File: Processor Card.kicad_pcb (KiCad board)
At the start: 2 copper layers, 100 x 100 mm, 33 parts, among them J1 Serial Port, J2 Conn_02x20_Odd_Even, U1 74LS32, U2 74LS04, U3 28C256 / 62256, U4 74LS73, U5 28C256 / 62256, U6 CDP1802/1806, U7 74LS373, U8 74LS138

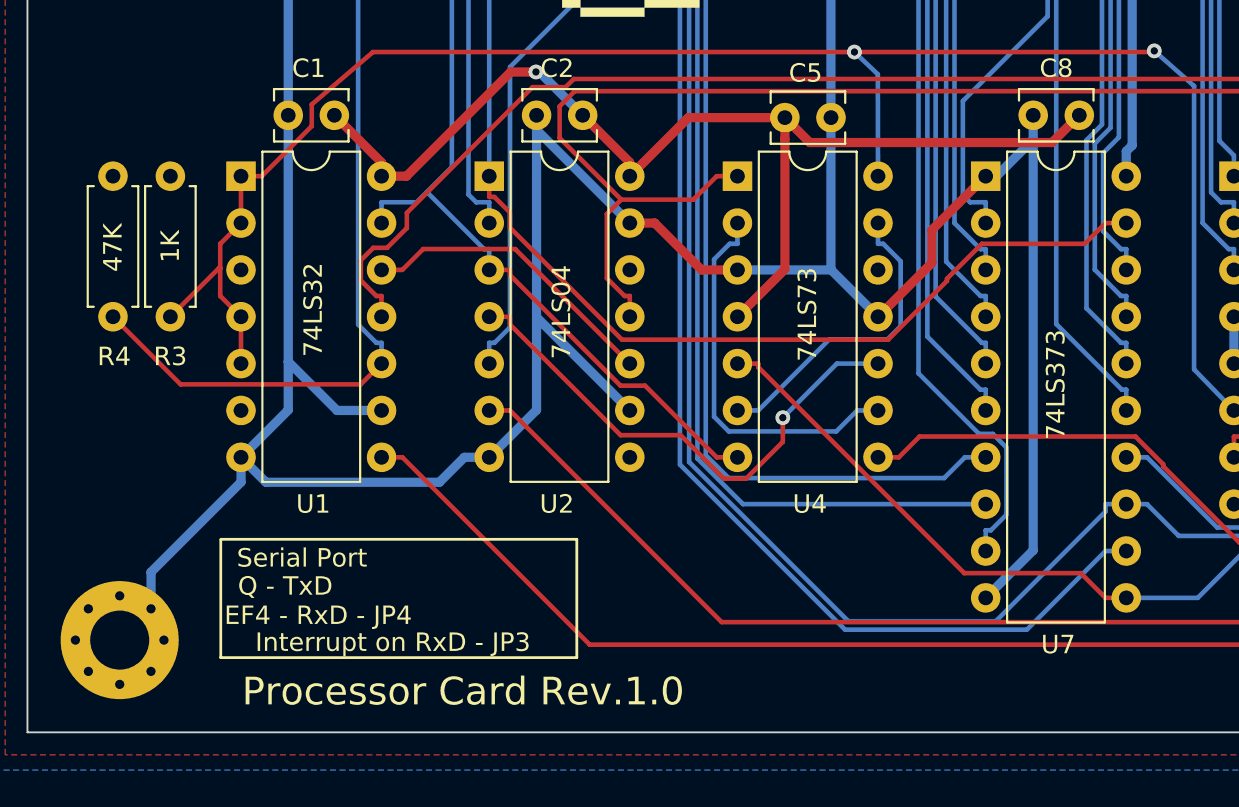
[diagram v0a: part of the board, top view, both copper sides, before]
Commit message: Added Gate Delay to IO Decode
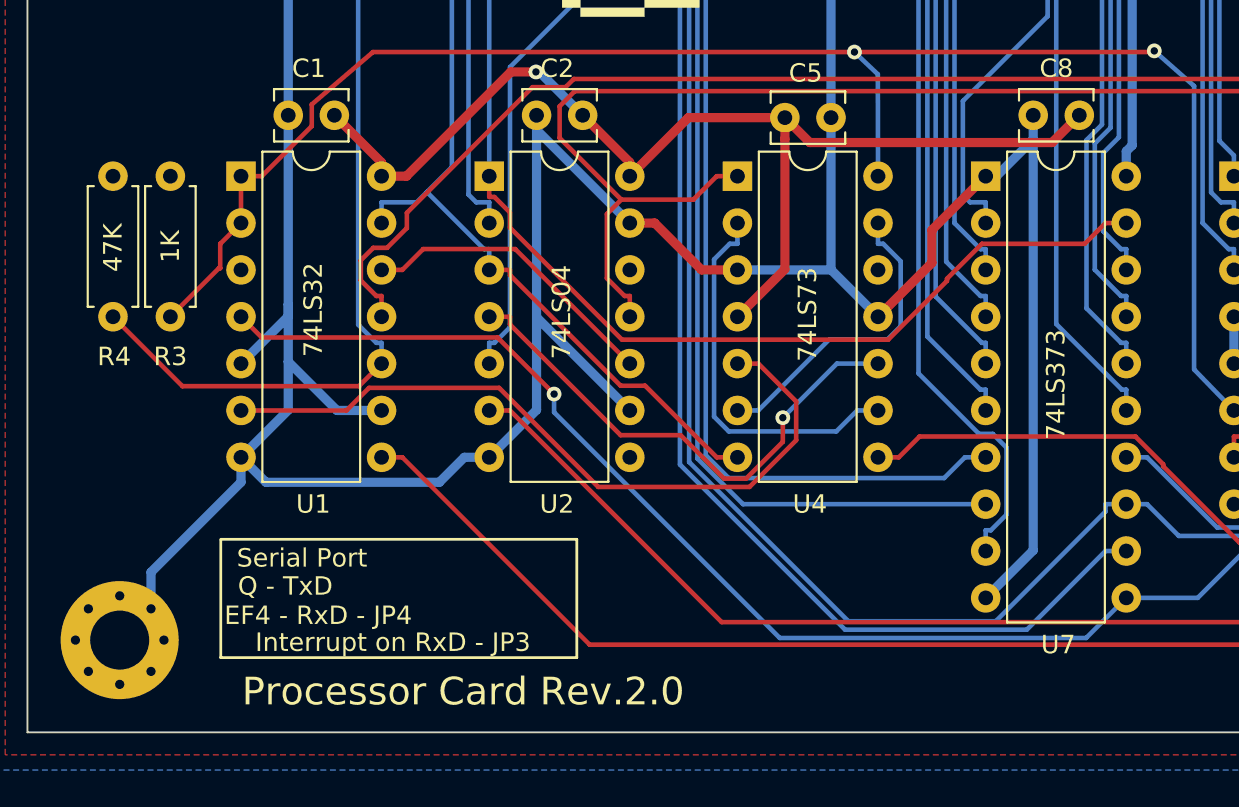
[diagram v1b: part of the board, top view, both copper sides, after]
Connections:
- U1 pad 4: HI -> TPA
- U1 pad 5: HI -> GND
- U4 pad 5: TPA -> Net-(U1-Pad6)
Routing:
- net Net-(U1-Pad6): track 0.00 -> 40.0 mm
- net TPA: track 121.1 -> 151.4 mm, vias 0 -> 1
- net HI: track 96.4 -> 90.8 mm
- net GND: track 508.8 -> 513.0 mm
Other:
- board text added: "Processor Card Rev.2.0"
- board text removed: "Processor Card Rev.1.0"
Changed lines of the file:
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@@
     (thickness 1.6)
     (drawings 23)
-    (tracks 1131)
+    (tracks 1142)
     (zones 0)
     (modules 33)
@@
       (net 67 "Net-(U4-Pad12)"))
     (pad 5 thru_hole oval (at 0 10.16) (size 1.6 1.6) (drill 0.8) (layers *.Cu *.Mask)
-      (net 20 TPA))
+      (net 72 "Net-(U1-Pad6)"))
     (pad 11 thru_hole oval (at 7.62 7.62) (size 1.6 1.6) (drill 0.8) (layers *.Cu *.Mask)
       (net 2 GND))
@@
       (net 69 "Net-(U1-Pad12)"))
     (pad 5 thru_hole oval (at 0 10.16) (size 1.6 1.6) (drill 0.8) (layers *.Cu *.Mask)
-      (net 78 HI))
+      (net 2 GND))
     (pad 11 thru_hole oval (at 7.62 7.62) (size 1.6 1.6) (drill 0.8) (layers *.Cu *.Mask)
       (net 10 ~IOW))
     (pad 4 thru_hole oval (at 0 7.62) (size 1.6 1.6) (drill 0.8) (layers *.Cu *.Mask)
-      (net 78 HI))
+      (net 20 TPA))
     (pad 10 thru_hole oval (at 7.62 10.16) (size 1.6 1.6) (drill 0.8) (layers *.Cu *.Mask)
       (net 75 /RX))
@@
     (effects (font (size 1 1) (thickness 0.15)))
   )
-  (gr_text "Processor Card Rev.1.0" (at 123.622 147.79) (layer F.SilkS)
+  (gr_text "Processor Card Rev.2.0" (at 123.622 147.79) (layer F.SilkS)
     (effects (font (size 1.5 1.5) (thickness 0.3)))
   )
@@
   (segment (start 119.196 132.55) (end 116.7805 132.55) (width 0.5) (layer B.Cu) (net 2) (status 10))
   (segment (start 114.137 129.9065) (end 114.137 132.529) (width 0.5) (layer B.Cu) (net 2))
-  (segment (start 114.137 116.548) (end 114.137 129.9065) (width 0.5) (layer B.Cu) (net 2) (status 10))
   (segment (start 112.9293 136.4433) (end 111.576 135.09) (width 0.5) (layer B.Cu) (net 2) (status 20))
   (segment (start 123.6827 135.09) (end 122.3294 136.4433) (width 0.5) (layer B.Cu) (net 2))
   (segment (start 122.3294 136.4433) (end 112.9293 136.4433) (width 0.5) (layer B.Cu) (net 2))
   (segment (start 125.033 135.09) (end 123.6827 135.09) (width 0.5) (layer B.Cu) (net 2) (status 10))
+  (segment (start 114.137 127.449) (end 114.137 126.795) (width 0.5) (layer B.Cu) (net 2))
+  (segment (start 111.576 130.01) (end 114.137 127.449) (width 0.5) (layer B.Cu) (net 2))
+  (segment (start 114.137 126.795) (end 114.137 129.9065) (width 0.5) (layer B.Cu) (net 2))
+  (segment (start 114.137 116.548) (end 114.137 126.795) (width 0.5) (layer B.Cu) (net 2))
   (segment (start 167.209 58.8256) (end 170.5633 55.4713) (width 0.5) (layer B.Cu) (net 3))
   (segment (start 170.5633 55.4713) (end 173.4163 55.4713) (width 0.5) (layer B.Cu) (net 3))
@@
   (segment (start 181.095 75.432) (end 181.095 76.5573) (width 0.25) (layer B.Cu) (net 20) (status 10))
   (segment (start 195.94 90.037) (end 195.3524 90.037) (width 0.25) (layer B.Cu) (net 20) (status 30))
-  (segment (start 138.49 130.01) (end 139.6153 130.01) (width 0.25) (layer F.Cu) (net 20) (status 10))
-  (segment (start 159.568 142.71) (end 158.4427 142.71) (width 0.25) (layer F.Cu) (net 20) (status 10))
-  (segment (start 158.4427 142.71) (end 157.102 141.3693) (width 0.25) (layer F.Cu) (net 20))
-  (segment (start 157.102 141.3693) (end 150.7856 141.3693) (width 0.25) (layer F.Cu) (net 20))
-  (segment (start 150.7856 141.3693) (end 139.6153 130.199) (width 0.25) (layer F.Cu) (net 20))
-  (segment (start 139.6153 130.199) (end 139.6153 130.01) (width 0.25) (layer F.Cu) (net 20))
+  (via (at 128.549 131.661) (size 0.8) (drill 0.4) (layers F.Cu B.Cu) (net 20))
+  (segment (start 128.549 132.651002) (end 128.549 131.661) (width 0.25) (layer B.Cu) (net 20))
+  (segment (start 140.782508 144.88451) (end 128.549 132.651002) (width 0.25) (layer B.Cu) (net 20))
+  (segment (start 157.39349 144.88451) (end 140.782508 144.88451) (width 0.25) (layer B.Cu) (net 20))
+  (segment (start 159.568 142.71) (end 157.39349 144.88451) (width 0.25) (layer B.Cu) (net 20))
+  (segment (start 112.701001 128.595001) (end 111.576 127.47) (width 0.25) (layer F.Cu) (net 20))
+  (segment (start 125.483001 128.595001) (end 112.701001 128.595001) (width 0.25) (layer F.Cu) (net 20))
+  (segment (start 128.549 131.661) (end 125.483001 128.595001) (width 0.25) (layer F.Cu) (net 20))
   (segment (start 155.3053 75.432) (end 157.8729 77.9996) (width 0.25) (layer F.Cu) (net 21))
   (segment (start 157.8729 77.9996) (end 162.1621 77.9996) (width 0.25) (layer F.Cu) (net 21))
@@
   (segment (start 195.5712 60.1462) (end 196.4877 61.0627) (width 0.25) (layer F.Cu) (net 70))
   (segment (start 196.4877 61.0627) (end 196.4877 61.43) (width 0.25) (layer F.Cu) (net 70))
+  (segment (start 117.29241 132.55) (end 111.576 132.55) (width 0.25) (layer F.Cu) (net 72))
+  (segment (start 125.569709 131.324999) (end 118.517411 131.324999) (width 0.25) (layer F.Cu) (net 72))
+  (segment (start 130.94172 136.69701) (end 125.569709 131.324999) (width 0.25) (layer F.Cu) (net 72))
+  (segment (start 118.517411 131.324999) (end 117.29241 132.55) (width 0.25) (layer F.Cu) (net 72))
+  (segment (start 139.1439 136.69701) (end 130.94172 136.69701) (width 0.25) (layer F.Cu) (net 72))
+  (segment (start 141.673601 134.167309) (end 139.1439 136.69701) (width 0.25) (layer F.Cu) (net 72))
+  (segment (start 141.673601 132.062231) (end 141.673601 134.167309) (width 0.25) (layer F.Cu) (net 72))
+  (segment (start 139.62137 130.01) (end 141.673601 132.062231) (width 0.25) (layer F.Cu) (net 72))
+  (segment (start 138.49 130.01) (end 139.62137 130.01) (width 0.25) (layer F.Cu) (net 72))
   (segment (start 181.4046 126.2929) (end 180.137 125.0253) (width 0.25) (layer B.Cu) (net 74))
   (segment (start 179.776 144.0247) (end 179.0116 143.2603) (width 0.25) (layer B.Cu) (net 74))
@@
   (segment (start 184.4733 54.0549) (end 191.4077 60.9893) (width 0.25) (layer B.Cu) (net 75))
   (segment (start 191.4077 60.9893) (end 191.4077 61.43) (width 0.25) (layer B.Cu) (net 75))
-  (segment (start 118.070999 131.135001) (end 119.196 130.01) (width 0.25) (layer F.Cu) (net 75))
-  (segment (start 108.300501 131.135001) (end 118.070999 131.135001) (width 0.25) (layer F.Cu) (net 75))
-  (segment (start 104.6355 127.47) (end 108.300501 131.135001) (width 0.25) (layer F.Cu) (net 75))
+  (segment (start 117.970999 131.235001) (end 119.196 130.01) (width 0.25) (layer F.Cu) (net 75))
+  (segment (start 108.400501 131.235001) (end 117.970999 131.235001) (width 0.25) (layer F.Cu) (net 75))
+  (segment (start 104.6355 127.47) (end 108.400501 131.235001) (width 0.25) (layer F.Cu) (net 75))
   (segment (start 186.106 137.503) (end 186.106 138.6283) (width 0.25) (layer B.Cu) (net 77) (status 10))
   (segment (start 187.396 145.25) (end 187.396 139.9183) (width 0.25) (layer B.Cu) (net 77) (status 10))
   (segment (start 187.396 139.9183) (end 186.106 138.6283) (width 0.25) (layer B.Cu) (net 77))
   (segment (start 111.576 122.39) (end 111.576 119.85) (width 0.25) (layer F.Cu) (net 78))
-  (segment (start 111.576 130.01) (end 111.576 127.47) (width 0.25) (layer F.Cu) (net 78))
   (segment (start 110.450999 123.515001) (end 111.576 122.39) (width 0.25) (layer F.Cu) (net 78))
-  (segment (start 111.576 127.47) (end 110.450999 126.344999) (width 0.25) (layer F.Cu) (net 78))
   (segment (start 110.377001 124.839999) (end 110.450999 124.839999) (width 0.25) (layer F.Cu) (net 78))
   (segment (start 107.747 127.47) (end 110.377001 124.839999) (width 0.25) (layer F.Cu) (net 78))
   (segment (start 110.450999 124.839999) (end 110.450999 123.515001) (width 0.25) (layer F.Cu) (net 78))
-  (segment (start 110.450999 126.344999) (end 110.450999 124.839999) (width 0.25) (layer F.Cu) (net 78))
   (segment (start 112.698 119.85) (end 111.576 119.85) (width 0.25) (layer F.Cu) (net 78))
   (segment (start 115.411999 117.136001) (end 112.698 119.85) (width 0.25) (layer F.Cu) (net 78))

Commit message: Sync
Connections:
- U1 pad 1: HI -> Net-(U1-Pad1)
- U1 pad 2: HI -> Net-(U1-Pad1)
- U1 pad 6: Net-(U1-Pad6) -> Net-(U1-Pad1)
- U4 pad 5: Net-(U1-Pad6) -> Net-(U1-Pad3)
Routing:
- net Net-(U1-Pad3): track 0.00 -> 51.6 mm, vias 0 -> 2
- net Net-(U1-Pad6): track 40.0 -> 0.00 mm
- net Net-(U1-Pad1): track 0.00 -> 13.7 mm
- net HI: track 90.8 -> 91.6 mm
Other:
- board text added: "Processor Card Rev.2.1"
- board text removed: "Processor Card Rev.2.0"

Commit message: Revision 2
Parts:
- removed D2: RED, LED_THT:LED_D3.0mm_Horizontal_O1.27mm_Z2.0mm
- removed the J1 at (185.0, 61.4)
- removed JP1, JP2: RAM ROM, Connector_PinHeader_2.54mm:PinHeader_1x03_P2.54mm_Vertical
- removed JP3: ~INT, Connector_PinHeader_2.54mm:PinHeader_1x02_P2.54mm_Vertical
- removed JP4: ~EF4, Connector_PinHeader_2.54mm:PinHeader_1x02_P2.54mm_Vertical
- removed R3: 1K, Resistor_THT:R_Axial_DIN0207_L6.3mm_D2.5mm_P7.62mm_Horizontal
- removed R4: 47K, Resistor_THT:R_Axial_DIN0207_L6.3mm_D2.5mm_P7.62mm_Horizontal
- removed the U8 at (165.4, 119.8)
- added C10: 100nF, Capacitor_THT:C_Disc_D3.8mm_W2.6mm_P2.50mm, F.Cu at (133.4, 121.8)
- added C11: 100nF, Capacitor_THT:C_Disc_D3.8mm_W2.6mm_P2.50mm, F.Cu at (149.6, 121.8)
- added C9: 100nF, Capacitor_THT:C_Disc_D3.8mm_W2.6mm_P2.50mm, F.Cu at (117.1, 121.8)
- added U10: 74LS573, Package_DIP:DIP-20_W7.62mm, F.Cu at (160.8, 101.4)
- added U11: 74LS138, Package_DIP:DIP-16_W7.62mm, F.Cu at (144.6, 125.6)
- added U3: 62256, Package_DIP:DIP-28_W15.24mm_Socket, F.Cu at (132.4, 59.5)
- added U5: 74LS32, Package_DIP:DIP-14_W7.62mm, F.Cu at (144.6, 101.4)
- D1: value GREEN -> LED
- R1: value 470R -> 1K
- U1: value 74LS32 -> CDP1802/1806; footprint Package_DIP:DIP-14_W7.62mm -> Package_DIP:DIP-40_W15.24mm_Socket
- U2: value 74LS04 -> 28C256; footprint Package_DIP:DIP-14_W7.62mm -> Package_DIP:DIP-28_W15.24mm_Socket
- U4: value 74LS73 -> 62256; footprint Package_DIP:DIP-14_W7.62mm -> Package_DIP:DIP-28_W15.24mm_Socket
- U6: renamed from U3; value 28C256 / 62256 -> 74LS20; footprint Package_DIP:DIP-28_W15.24mm_Socket -> Package_DIP:DIP-14_W7.62mm
- U7: value 74LS373 -> 74LS74; footprint Package_DIP:DIP-20_W7.62mm -> Package_DIP:DIP-14_W7.62mm
- U8: renamed from U5; value 28C256 / 62256 -> 74LS04; footprint Package_DIP:DIP-28_W15.24mm_Socket -> Package_DIP:DIP-14_W7.62mm
- U9: renamed from U6; value CDP1802/1806 -> 74LS74; footprint Package_DIP:DIP-40_W15.24mm_Socket -> Package_DIP:DIP-14_W7.62mm
- moved U1 86.1 mm to (173.0, 59.5)
- moved U6 70.7 mm to (112.1, 125.6)
- moved U4 62.0 mm to (152.7, 59.5)
- moved C4 61.9 mm to (181.9, 55.7)
- moved C2 61.8 mm to (141.3, 55.7)
- moved U2 61.7 mm to (112.1, 59.5)
- moved C1 61.0 mm to (120.9, 55.7)
- moved U9 55.8 mm to (128.3, 101.4)
- moved G*** 50.2 mm to (176.2, 135.1)
- moved C7 47.9 mm to (149.6, 97.6)
- moved C6 42.7 mm to (133.4, 97.6)
- moved U8 41.2 mm to (112.1, 101.4)
- moved C5 30.6 mm to (117.1, 97.6), turned to 180 degrees
- moved U7 24.3 mm to (128.3, 125.6)
- moved C8 20.9 mm to (165.9, 97.6)
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- renumbered C9 to C12, J2 to J1
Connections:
- J1 pad 10: ~INTERRUPT -> ~{INTERRUPT}
- J1 pad 12: ~MWR -> ~{MWR}
- J1 pad 13: ~MRD -> ~{MRD}
- J1 pad 15: Net-(J2-Pad15) -> unconnected-(J1-Pad15)
- J1 pad 25: ~IOW -> ~{IOW}
- J1 pad 26: ~IOR -> ~{IOR}
- J1 pad 27: ~N7 -> ~{N7}
- J1 pad 28: ~N6 -> ~{N6}
- J1 pad 29: ~N5 -> ~{N5}
- J1 pad 3: ~WAIT -> ~{WAIT}
- J1 pad 30: ~N4 -> ~{N4}
- J1 pad 31: ~N3 -> ~{N3}
- J1 pad 32: ~N2 -> ~{N2}
- J1 pad 33: ~N1 -> ~{N1}
- J1 pad 34: Net-(J2-Pad34) -> unconnected-(J1-Pad34)
- J1 pad 35: ~EF1 -> ~{EF1}
- J1 pad 36: ~EF2 -> ~{EF2}
- J1 pad 37: ~EF3 -> ~{EF3}
- J1 pad 38: ~EF4 -> ~{EF4}
- J1 pad 5: ~CLEAR -> ~{CLEAR}
- J1 pad 6: ~DMA_IN -> ~{DMA_IN}
- J1 pad 8: ~DMA_OUT -> ~{DMA_OUT}
- R1 pad 2: Net-(D1-Pad2) -> HI
- R2 pad 2: Net-(D2-Pad2) -> Net-(D1-Pad2)
- U1 pad 1: Net-(U1-Pad1) -> CLOCK
- U1 pad 10: /RX -> D5
- U1 pad 11: ~IOW -> D4
- U1 pad 12: Net-(U1-Pad12) -> D3
- U1 pad 13: ~MRD -> D2
- U1 pad 14: VCC -> D1
- U1 pad 2: Net-(U1-Pad1) -> ~{WAIT}
- U1 pad 3: Net-(U1-Pad3) -> ~{CLEAR}
- U1 pad 4: TPA -> Q
- U1 pad 5: GND -> SC1
- U1 pad 6: Net-(U1-Pad1) -> SC0
- U1 pad 7: GND -> ~{MRD}
- U1 pad 8: Net-(D1-Pad1) -> D7
- U1 pad 9: GND -> D6
- U2 pad 1: /A15 -> /A14
- U2 pad 10: Net-(U1-Pad12) -> /A0
- U2 pad 11: TPB -> D0
- U2 pad 12: Net-(U2-Pad12) -> D1
- U2 pad 13: GND -> D2
- U2 pad 14: VCC -> GND
- U2 pad 2: Net-(U2-Pad2) -> /A12
- U2 pad 3: ~MRD -> /A7
- U2 pad 4: Net-(U2-Pad4) -> /A6
- U2 pad 5: Q -> /A5
- U2 pad 6: /TX -> /A4
- U2 pad 7: GND -> /A3
- U2 pad 8: Net-(U2-Pad8) -> /A2
- U2 pad 9: GND -> /A1
- U4 pad 1: TPB -> /A14
- U4 pad 10: Net-(U2-Pad4) -> /A0
- U4 pad 11: GND -> D0
- U4 pad 12: Net-(U4-Pad12) -> D1
- U4 pad 13: Net-(U4-Pad13) -> D2
- U4 pad 14: HI -> GND
- U4 pad 2: Net-(U4-Pad2) -> /A12
- U4 pad 3: GND -> /A7
- U4 pad 4: VCC -> /A6
- U4 pad 5: Net-(U1-Pad3) -> /A5
- U4 pad 6: Net-(U4-Pad13) -> /A4
- U4 pad 7: ~MRD -> /A3
- U4 pad 8: ~IOR -> /A2
- U4 pad 9: Net-(U4-Pad2) -> /A1
- U6 pad 1: /A14 -> Net-(U6-Pad1)
- U6 pad 10: /A0 -> GND
- U6 pad 11: D0 -> (no net)
- U6 pad 12: D1 -> GND
- U6 pad 13: D2 -> GND
- U6 pad 14: GND -> VCC
- U6 pad 2: /A12 -> Net-(U6-Pad2)
- U6 pad 3: /A7 -> (no net)
- U6 pad 4: /A6 -> A15
- U6 pad 5: /A5 -> TPB
- U6 pad 6: /A4 -> Net-(U6-Pad6)
- U6 pad 7: /A3 -> GND
- U6 pad 8: /A2 -> unconnected-(U6-Pad8)
- U6 pad 9: /A1 -> GND
- U7 pad 1: GND -> ~{CLEAR}
- U7 pad 10: GND -> HI
- U7 pad 11: TPA -> HI
- U7 pad 12: /A12 -> HI
- U7 pad 13: /A4 -> HI
- U7 pad 14: /A5 -> VCC
- U7 pad 2: /A8 -> GND
- U7 pad 3: /A0 -> GND
- U7 pad 4: /A1 -> Net-(U6-Pad6)
- U7 pad 5: /A9 -> Net-(U5-Pad2)
- U7 pad 6: /A10 -> Net-(U5-Pad4)
- U7 pad 7: /A2 -> GND
- U7 pad 8: /A3 -> unconnected-(U7-Pad8)
- U7 pad 9: /A11 -> unconnected-(U7-Pad9)
- U8 pad 1: /A14 -> SC0
- U8 pad 10: /A0 -> Net-(U8-Pad10)
- U8 pad 11: D0 -> TPA
- U8 pad 12: D1 -> Net-(D1-Pad1)
- U8 pad 13: D2 -> Q
- U8 pad 14: GND -> VCC
- U8 pad 2: /A12 -> Net-(U6-Pad1)
- U8 pad 3: /A7 -> SC1
- U8 pad 4: /A6 -> Net-(U6-Pad2)
- U8 pad 5: /A5 -> A15
- U8 pad 6: /A4 -> /Memory Select/~{HI RAM CS}
- U8 pad 7: /A3 -> GND
- U8 pad 8: /A2 -> Net-(U5-Pad9)
- U8 pad 9: /A1 -> TPB
- U9 pad 1: CLOCK -> Net-(U9-Pad1)
- U9 pad 10: D5 -> GND
- U9 pad 11: D4 -> Net-(U5-Pad9)
- U9 pad 12: D3 -> HI
- U9 pad 13: D2 -> ~{IOR}
- U9 pad 14: D1 -> VCC
- U9 pad 2: ~WAIT -> ~{MRD}
- U9 pad 3: ~CLEAR -> Net-(U8-Pad10)
- U9 pad 4: Q -> GND
- U9 pad 5: SC1 -> unconnected-(U9-Pad5)
- U9 pad 6: SC0 -> ~{IOR}
- U9 pad 7: ~MRD -> GND
- U9 pad 8: D7 -> unconnected-(U9-Pad8)
- U9 pad 9: D6 -> Net-(U9-Pad1)
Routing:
- net ~{CLEAR}: track 0.00 -> 160.8 mm
- net /RX: track 159.9 -> 0.00 mm
- net /TX: track 155.9 -> 0.00 mm
- net ~MRD: track 150.4 -> 0.00 mm, vias 1 -> 0
- net ~{MRD}: track 0.00 -> 133.8 mm, vias 0 -> 1
- net A15: track 0.00 -> 104.1 mm
- net VCC: track 246.5 -> 347.3 mm, vias 1 -> 0
- net SC1: track 33.6 -> 131.4 mm, vias 0 -> 1
- net ~MWR: track 89.7 -> 0.00 mm
- net /Memory Select/~{HI RAM CS}: track 0.00 -> 89.6 mm, vias 0 -> 1
- net ~IOW: track 87.5 -> 0.00 mm
- net /A15: track 82.5 -> 0.00 mm
- net ~IOR: track 80.5 -> 0.00 mm
- net SC0: track 33.6 -> 111.9 mm, vias 0 -> 1
- net ~{IOR}: track 0.00 -> 75.8 mm, vias 0 -> 1
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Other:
- net class Default removed
- net class Power removed
- board text added: "Processor Card Rev.2"
- board text removed: "0 - 32K"
- board text removed: "32 - 64K"
- board text removed: "CTS"
- board text removed: "EF4 - RxD - JP4"
- board text removed: "GND"
- board text removed: "Interrupt on RxD - JP3"
- board text removed: "Processor Card Rev.2.1"
- board text removed: "Q - TxD"
- board text removed: "RTS"
- board text removed: "RX"
- board text removed: "Serial Port"
- board text removed: "TX"
- board text removed: "VCC"
